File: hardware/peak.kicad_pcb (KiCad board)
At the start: 6 copper layers, 35 x 51 mm, 29 parts, among them J1 Conn_Controller, J2 Conn_Buttons, J3 Conn_CAN, J4 Conn_Display, J5 Conn_DEBUG, Q1 AO3400A, U1 ESP32-S3-WROOM-1, U2 TLV76733DRVx, U3 MCP2542FDxMF

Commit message: ✨ Further schematic updates
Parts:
- removed C1, C2, C3: 10uF/10V, Capacitor_SMD:C_0805_2012Metric
- removed C10, C8, C9: 100nF, Capacitor_SMD:C_0603_1608Metric
- removed C4: 1uF, Capacitor_SMD:C_0603_1608Metric
- removed C7: 1uF/10V, Capacitor_SMD:C_0805_2012Metric
- removed J1: Conn_Controller, Connector_Molex:Molex_PicoBlade_53261-0471_1x04-1MP_P1.25mm_Horizontal
- removed J2: Conn_Buttons, Connector_Molex:Molex_PicoBlade_53261-0471_1x04-1MP_P1.25mm_Horizontal
- removed J3: Conn_CAN, Connector_Molex:Molex_PicoBlade_53261-0271_1x02-1MP_P1.25mm_Horizontal
- removed J4: Conn_Display, lib:ST7789V2
- removed J5: Conn_DEBUG, lib:DEBUG_SMD
- removed Q1: AO3400A, PCM_Package_TO_SOT_SMD_AKL:SOT-23
- removed R2: 10k, PCM_Resistor_SMD_AKL:R_0603_1608Metric
- removed R4: 5R, PCM_Resistor_SMD_AKL:R_0805_2012Metric
- added U4: TPS62A04ADRL, Package_TO_SOT_SMD:SOT-563, F.Cu at (21.8, 16.8)
- added U6: AP3019AKTR, Package_TO_SOT_SMD:SOT-23-6, F.Cu at (17.1, 22.2)
- added U7: W25Q128JVP, Package_SON:WSON-8-1EP_6x5mm_P1.27mm_EP3.4x4.3mm, F.Cu at (3.73, 15.0)
- added U8: MCP1700T-2502E-TT, PCM_Package_TO_SOT_SMD_AKL:SOT-23, F.Cu at (22.0, 22.2)
- U1: value ESP32-S3-WROOM-1 -> ~; footprint RF_Module:ESP32-S3-WROOM-1 -> PCM_Espressif:ESP32-P4
- U2: value TLV76733DRVx -> AP63203WU; footprint Package_SON:WSON-6-1EP_2x2mm_P0.65mm_EP1x1.6mm_ThermalVias -> PCM_Package_TO_SOT_SMD_AKL:TSOT-23-6
- moved U1 168.0 mm to (6.40, 5.62)
- moved R1 167.5 mm to (16.6, 0.86), turned to 0 degrees
- moved R3 166.0 mm to (16.6, 3.58), turned to 0 degrees
- moved U2 160.9 mm to (17.3, 17.5)
- moved C5 159.7 mm to (20.6, 0.76), turned to 0 degrees
- moved C6 159.0 mm to (20.6, 3.27), turned to 0 degrees
- moved U3 158.0 mm to (25.8, 1.88), turned to 0 degrees
- moved R5 149.2 mm to (16.6, 6.30), turned to 0 degrees
- moved R6 148.6 mm to (16.6, 9.02), turned to 0 degrees
- moved R7 148.0 mm to (16.6, 11.7), turned to 0 degrees
- moved C11 143.5 mm to (20.6, 5.78), turned to 0 degrees
- moved C12 142.9 mm to (20.6, 8.29), turned to 0 degrees
- moved C13 142.3 mm to (20.6, 10.8), turned to 0 degrees
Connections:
- U1 pad 1: GND -> unconnected-(U1-GPIO1/ADC-Pad1)
- U1 pad 10: /TXD -> unconnected-(U1-GPIO9/ADC-Pad10)
- U1 pad 11: /RXD -> unconnected-(U1-GPIO10/ADC-Pad11)
- U1 pad 12: /BACKLIGHT -> unconnected-(U1-GPIO11/ADC-Pad12)
- U1 pad 18: /CS -> unconnected-(U1-GPIO17/ADC-Pad18)
- U1 pad 19: /SDA -> unconnected-(U1-GPIO18/ADC-Pad19)
- U1 pad 2: +3.3V -> unconnected-(U1-GPIO2/ADC-Pad2)
- U1 pad 20: /SCL -> unconnected-(U1-GPIO19/ADC-Pad20)
- U1 pad 21: unconnected-(U1-IO13-Pad21) -> +3.3V
- U1 pad 26: unconnected-(U1-IO45-Pad26) -> +1V2
- U1 pad 27: /BOOT -> /MCU/FLASH_CS
- U1 pad 28: unconnected-(U1-IO35-Pad28) -> /MCU/FLASH_Q
- U1 pad 29: unconnected-(U1-IO36-Pad29) -> /MCU/FLASH_WP
- U1 pad 3: /EN -> unconnected-(U1-GPIO3/ADC-Pad3)
- U1 pad 30: unconnected-(U1-IO37-Pad30) -> +3.3V
- U1 pad 31: unconnected-(U1-IO38-Pad31) -> /MCU/FLASH_HOLD
- U1 pad 32: unconnected-(U1-IO39-Pad32) -> /MCU/FLASH_CK
- U1 pad 33: unconnected-(U1-IO40-Pad33) -> /MCU/FLASH_D
- U1 pad 36: /RX0 -> unconnected-(U1-DSI_DATAN1-Pad36)
- U1 pad 37: /TX0 -> unconnected-(U1-DSI_CLKN-Pad37)
- U1 pad 38: /DC -> unconnected-(U1-DSI_CLKP-Pad38)
- U1 pad 4: /RESET -> unconnected-(U1-GPIO4/ADC-Pad4)
- U1 pad 40: GND -> unconnected-(U1-DSI_DATAN0-Pad40)
- U1 pad 41: GND -> +2V5
- U1 pad 5: /BUTTON_D -> unconnected-(U1-GPIO5/ADC-Pad5)
- U1 pad 6: /BUTTON_U -> unconnected-(U1-GPIO6/ADC-Pad6)
- U1 pad 7: /BUTTON_P -> unconnected-(U1-GPIO7/ADC-Pad7)
- U1 pad 9: unconnected-(U1-IO16-Pad9) -> +3.3V
- U2 pad 2: +3.3V -> +5V
- U2 pad 3: GND -> +5V
- U2 pad 4: +5V -> GND
- U2 pad 5: GND -> Net-(U2-SW)
- U2 pad 6: +5V -> Net-(U2-BST)
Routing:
- net /BUTTON_D: track 48.6 -> 0.00 mm, vias 2 -> 0
- net /BUTTON_U: track 47.3 -> 0.00 mm, vias 2 -> 0
- net /BUTTON_P: track 45.9 -> 0.00 mm, vias 2 -> 0
- net /CAN_L: track 41.0 -> 0.00 mm, vias 2 -> 0
- net /CAN_H: track 40.9 -> 0.00 mm
- net /DC: track 33.3 -> 0.00 mm, vias 1 -> 0
- net /RESET: track 29.9 -> 0.00 mm, vias 1 -> 0
- net /EN: track 28.4 -> 0.00 mm, vias 2 -> 0
- net +3.3V: track 18.3 -> 0.00 mm, vias 7 -> 0
- net /TXD: track 18.3 -> 0.00 mm, vias 2 -> 0
- net /RXD: track 18.0 -> 0.00 mm, vias 2 -> 0
- net /SDA: track 13.7 -> 0.00 mm, vias 1 -> 0
- net /CS: track 12.7 -> 0.00 mm, vias 1 -> 0
- net /BOOT: track 12.7 -> 0.00 mm
- net /SCL: track 12.2 -> 0.00 mm, vias 1 -> 0
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- removed copper zone on F.Cu, net +3.3V
- removed copper zone on In3.Cu, net +3.3V
- removed copper zone on F.Cu, net +5V
- removed copper zone on In3.Cu, net +5V
- removed copper zone on B.Cu, net GND
- removed copper zone on F.Cu, net GND
- removed copper zone on In1.Cu, net GND
- removed copper zone on In4.Cu, net GND
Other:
- board outline removed
- copper layers 6 -> 4
- board text removed: "3.3V"
- board text removed: "BUTTONS"
- board text removed: "CAN"
- board text removed: "CTRL"
- board text removed: "DEBUG"
- board text removed: "LED"

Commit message: 📂 PCB updates
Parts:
- added C1: 10uF, Capacitor_SMD:C_0805_2012Metric, F.Cu at (188.4, 79.9)
- added C14: 100nF/100V, Capacitor_SMD:C_0805_2012Metric, F.Cu at (193.1, 106.8)
- added C15: 10uF/100V, Capacitor_SMD:C_1206_3216Metric, F.Cu at (189.7, 101.7)
- added C16: 10uF/100V, Capacitor_SMD:C_1206_3216Metric, F.Cu at (189.7, 104.0)
- added C17: 100nF/100V, Capacitor_SMD:C_0805_2012Metric, F.Cu at (188.3, 92.7)
- added C18: 1uF, Capacitor_SMD:C_0402_1005Metric, F.Cu at (201.1, 88.1)
- added C2: 100nF/50V, Capacitor_SMD:C_0603_1608Metric, F.Cu at (190.9, 79.6)
- added C20: 22uF, Capacitor_SMD:C_0805_2012Metric, F.Cu at (194.9, 89.0)
- added C21: 22uF, Capacitor_SMD:C_0805_2012Metric, F.Cu at (194.9, 87.0)
- added C22: 22uF, Capacitor_SMD:C_0805_2012Metric, F.Cu at (194.9, 85.0)
- added C23: 10uF, Capacitor_SMD:C_0805_2012Metric, F.Cu at (227.9, 78.9)
- added C24: 4.7nF, Capacitor_SMD:C_0603_1608Metric, F.Cu at (224.2, 79.1)
- added C25: 22uF, Capacitor_SMD:C_0805_2012Metric, F.Cu at (226.0, 85.0)
- added C26: 22uF, Capacitor_SMD:C_0805_2012Metric, F.Cu at (228.0, 85.0)
- added C27: 4.7uF, Capacitor_SMD:C_0603_1608Metric, F.Cu at (228.8, 90.2)
- added C28: 0.22uF/50V, Capacitor_SMD:C_0805_2012Metric, F.Cu at (228.5, 93.5)
- added C29: 100nF, Capacitor_SMD:C_0402_1005Metric, F.Cu at (202.6, 98.2)
- added C3: 22uF, Capacitor_SMD:C_0805_2012Metric, F.Cu at (195.1, 80.6)
- added C30: 1uF, Capacitor_SMD:C_0603_1608Metric, F.Cu at (221.4, 83.6)
- added C31: 1uF, Capacitor_SMD:C_0603_1608Metric, F.Cu at (216.3, 83.6)
- added C32: 1uF, Capacitor_SMD:C_0603_1608Metric, F.Cu at (198.8, 81.0)
- added C33: 4.7uF, Capacitor_SMD:C_0603_1608Metric, F.Cu at (198.8, 83.0)
- added C34: 100nF, Capacitor_SMD:C_0603_1608Metric, F.Cu at (228.7, 122.3)
- added C35: 100nF, Capacitor_SMD:C_0603_1608Metric, F.Cu at (228.7, 125.3)
- added C36: 100nF, Capacitor_SMD:C_0603_1608Metric, F.Cu at (228.7, 123.8)
- added C37: 100nF, Capacitor_SMD:C_0603_1608Metric, F.Cu at (226.3, 128.2)
- added C38: 100nF, Capacitor_SMD:C_0603_1608Metric, B.Cu at (211.1, 64.0)
- added C39: 12pF, Capacitor_SMD:C_0402_1005Metric, F.Cu at (203.1, 82.8)
- added C4: 22uF, Capacitor_SMD:C_0805_2012Metric, F.Cu at (193.0, 80.5)
- added C40: 12pF, Capacitor_SMD:C_0402_1005Metric, F.Cu at (207.2, 82.8)
- added C41: 1uF, Capacitor_SMD:C_0402_1005Metric, F.Cu at (216.4, 91.1)
- added C42: 1uF, Capacitor_SMD:C_0402_1005Metric, F.Cu at (216.4, 90.1)
- added C43: 1uF, Capacitor_SMD:C_0402_1005Metric, F.Cu at (216.4, 89.1)
- added C44: 1uF, Capacitor_SMD:C_0402_1005Metric, F.Cu at (216.4, 88.1)
- added C45: 100nF, Capacitor_SMD:C_0402_1005Metric, F.Cu at (213.6, 99.3)
- added C46: 100nF, Capacitor_SMD:C_0402_1005Metric, F.Cu at (213.9, 84.6)
- added C47: 100nF, Capacitor_SMD:C_0402_1005Metric, F.Cu at (216.4, 93.1)
- added C48: 100nF, Capacitor_SMD:C_0402_1005Metric, F.Cu at (216.4, 95.1)
- added C49: 100nF, Capacitor_SMD:C_0402_1005Metric, F.Cu at (209.4, 84.6)
- added C50: 100nF, Capacitor_SMD:C_0402_1005Metric, F.Cu at (201.1, 91.1)
- added C51: 100nF, Capacitor_SMD:C_0402_1005Metric, F.Cu at (216.4, 94.1)
- added C52: 100nF, Capacitor_SMD:C_0402_1005Metric, F.Cu at (212.6, 99.3)
- added C53: 100nF, Capacitor_SMD:C_0402_1005Metric, F.Cu at (210.4, 84.6)
- added C54: 100nF, Capacitor_SMD:C_0402_1005Metric, F.Cu at (201.1, 89.1)
- added C55: 100nF, Capacitor_SMD:C_0402_1005Metric, F.Cu at (212.9, 84.6)
- added C56: 100nF, Capacitor_SMD:C_0402_1005Metric, F.Cu at (216.4, 87.1)
- added C57: 100nF, Capacitor_SMD:C_0402_1005Metric, F.Cu at (201.1, 86.1)
- added C58: 100nF, Capacitor_SMD:C_0402_1005Metric, F.Cu at (201.1, 85.1)
- added C59: 100nF, Capacitor_SMD:C_0402_1005Metric, F.Cu at (208.4, 84.6)
- added C60: 100nF, Capacitor_SMD:C_0402_1005Metric, F.Cu at (201.1, 90.1)
- added C61: 10uF, Capacitor_SMD:C_0603_1608Metric, F.Cu at (199.5, 71.3)
- added C62: 1uF, Capacitor_SMD:C_0603_1608Metric, F.Cu at (199.5, 76.0)
- added C7: 1uF/100V, Capacitor_SMD:C_1206_3216Metric, F.Cu at (188.5, 97.2)
- added C8: 1uF/100V, Capacitor_SMD:C_1206_3216Metric, F.Cu at (190.8, 97.2)
- added C9: 1uF/100V, Capacitor_SMD:C_1206_3216Metric, F.Cu at (193.1, 97.2)
- added DZ1: BZX84-C12, PCM_Package_TO_SOT_SMD_AKL:SOT-23, F.Cu at (193.0, 118.7)
- added F2: Fuse, Fuse:Fuse_2512_6332Metric_Pad1.52x3.35mm_HandSolder, F.Cu at (191.4, 110.5)
- added FB1: FerriteBead, Inductor_SMD:L_0805_2012Metric, F.Cu at (201.2, 82.0)
- added FL1: ACT32P-102-2P-TL01, PEAK:ACT32P_TDK, F.Cu at (189.7, 106.9)
- added J1: ~, lib:5034802000, F.Cu at (208.8, 104.4)
- added J2: Conn_DEBUG_C6, Connector_JST:JST_SHL_SM06B-SHLS-TF_1x06-1MP_P1.00mm_Horizontal, F.Cu at (192.2, 71.1)
- added J3: Conn_Buttons, Connector_JST:JST_PH_S4B-PH-SM4-TB_1x04-1MP_P2.00mm_Horizontal, F.Cu at (217.0, 124.8)
- added J4: Conn_DEBUG_P4, Connector_JST:JST_SHL_SM06B-SHLS-TF_1x06-1MP_P1.00mm_Horizontal, F.Cu at (225.4, 71.1)
- added J6: Conn_Controller, Connector_JST:JST_PH_S5B-PH-SM4-TB_1x05-1MP_P2.00mm_Horizontal, F.Cu at (202.5, 124.8)
- added L1: 8.2uH, Inductor_SMD:L_Bourns_SRP5030T, F.Cu at (190.3, 86.9)
- added L2: 3.9uH, Inductor_SMD:L_APV_ANR4030, F.Cu at (194.2, 76.5)
- added L3: 220nH, Inductor_SMD:L_0603_1608Metric, F.Cu at (226.6, 81.7)
- added L4: 15uH, Inductor_SMD:L_1210_3225Metric, F.Cu at (225.7, 90.2)
- added Q1: DMP10H400SE, PCM_Package_TO_SOT_SMD_AKL:SOT-223-3_TabPin2, F.Cu at (191.1, 125.2)
- added Q2: BSS123, PCM_Package_TO_SOT_SMD_AKL:SOT-23, F.Cu at (189.2, 118.7)
- added R10: 100k, Resistor_SMD:R_0603_1608Metric, F.Cu at (224.2, 85.2)
- added R11: 10, Resistor_SMD:R_0805_2012Metric, F.Cu at (225.1, 96.2)
- added R12: 100k, Resistor_SMD:R_0603_1608Metric, F.Cu at (228.3, 96.0)
- added R13: 10k, PCM_Resistor_SMD_AKL:R_0402_1005Metric, F.Cu at (201.1, 92.1)
- added R14: 10k, Resistor_SMD:R_0603_1608Metric, F.Cu at (225.7, 122.3)
- added R15: 10k, Resistor_SMD:R_0603_1608Metric, F.Cu at (225.7, 125.3)
- added R16: 10k, Resistor_SMD:R_0603_1608Metric, F.Cu at (225.7, 123.8)
- added R17: 10k, Resistor_SMD:R_0603_1608Metric, F.Cu at (188.9, 116.0)
- added R18: 1M, Resistor_SMD:R_0603_1608Metric, F.Cu at (198.6, 106.0)
- added R19: 47k, Resistor_SMD:R_0603_1608Metric, F.Cu at (198.6, 103.0)
- added R2: 100k, Resistor_SMD:R_0603_1608Metric, F.Cu at (194.1, 90.9)
- added R20: 1k, Resistor_SMD:R_0603_1608Metric, F.Cu at (197.1, 106.0)
- added R21: 0, PCM_Resistor_SMD_AKL:R_0402_1005Metric, F.Cu at (204.2, 85.0)
- added R22: 0, PCM_Resistor_SMD_AKL:R_0402_1005Metric, F.Cu at (206.1, 85.0)
- added R23: 4.02k, PCM_Resistor_SMD_AKL:R_0402_1005Metric, F.Cu at (205.3, 99.3)
- added R24: 10k, Resistor_SMD:R_0603_1608Metric, F.Cu at (199.5, 74.5)
- added R25: 10k, Resistor_SMD:R_0603_1608Metric, F.Cu at (211.9, 81.5)
- added R26: 0, Resistor_SMD:R_0603_1608Metric, F.Cu at (219.5, 107.4)
- added R27: 0, Resistor_SMD:R_0603_1608Metric, F.Cu at (221.0, 107.4)
- added R28: 0, Resistor_SMD:R_0603_1608Metric, F.Cu at (225.8, 107.4)
- added R29: 0, Resistor_SMD:R_0603_1608Metric, F.Cu at (227.3, 107.4)
- added R30: 51k, Resistor_SMD:R_0603_1608Metric, F.Cu at (218.1, 77.2)
- added R31: 51k, Resistor_SMD:R_0603_1608Metric, F.Cu at (218.1, 75.7)
- added R32: 51k, Resistor_SMD:R_0603_1608Metric, F.Cu at (218.1, 74.2)
- added R33: 51k, Resistor_SMD:R_0603_1608Metric, F.Cu at (218.1, 72.7)
- added R34: 51k, Resistor_SMD:R_0603_1608Metric, F.Cu at (218.1, 78.7)
- added R35: 51k, Resistor_SMD:R_0603_1608Metric, F.Cu at (213.4, 81.5)
- added R36: 0, PCM_Resistor_SMD_AKL:R_0402_1005Metric, F.Cu at (206.3, 99.3)
- added R37: 0, PCM_Resistor_SMD_AKL:R_0402_1005Metric, F.Cu at (207.3, 99.3)
- added R38: 0, PCM_Resistor_SMD_AKL:R_0402_1005Metric, F.Cu at (208.3, 99.3)
- added R39: 0, PCM_Resistor_SMD_AKL:R_0402_1005Metric, F.Cu at (209.3, 99.3)
- added R4: 19.1k, Resistor_SMD:R_0603_1608Metric, F.Cu at (193.5, 93.4)
- added R40: 0, PCM_Resistor_SMD_AKL:R_0402_1005Metric, F.Cu at (210.6, 99.3)
- added R41: 0, PCM_Resistor_SMD_AKL:R_0402_1005Metric, F.Cu at (211.6, 99.3)
- added R42: 4.7k, PCM_Resistor_SMD_AKL:R_0402_1005Metric, F.Cu at (219.3, 94.0)
- added R43: 4.7k, PCM_Resistor_SMD_AKL:R_0402_1005Metric, F.Cu at (219.3, 95.1)
- added R44: 10k, PCM_Resistor_SMD_AKL:R_0402_1005Metric, F.Cu at (201.1, 87.1)
- added R45: 10k, PCM_Resistor_SMD_AKL:R_0402_1005Metric, F.Cu at (216.4, 92.1)
- added R8: 0, Resistor_SMD:R_0603_1608Metric, F.Cu at (192.8, 103.6)
- added R9: 100k, Resistor_SMD:R_0603_1608Metric, F.Cu at (224.2, 82.2)
- added TP1: 5V, TestPoint:TestPoint_Pad_D1.0mm, F.Cu at (198.2, 90.5)
- added TP2: 3.3V, TestPoint:TestPoint_Pad_D1.0mm, F.Cu at (197.8, 78.0)
- added TP3: 1.2V, TestPoint:TestPoint_Pad_D1.0mm, F.Cu at (230.2, 83.9)
- added TP4: LEDA, TestPoint:TestPoint_Pad_D1.0mm, F.Cu at (230.9, 92.5)
- added TP5: 2.5V, TestPoint:TestPoint_Pad_D1.0mm, F.Cu at (218.9, 80.6)
- added TP6: 3.3VA, TestPoint:TestPoint_Pad_D1.0mm, F.Cu at (198.3, 84.9)
- added TP7: VIN, TestPoint:TestPoint_Pad_D1.0mm, F.Cu at (208.8, 129.7)
- added TP8: VBUS, TestPoint:TestPoint_Pad_D1.0mm, F.Cu at (196.8, 110.2)
- added TP9: GND, TestPoint:TestPoint_Pad_D1.0mm, F.Cu at (210.3, 117.9)
- added U10: STS4X, PEAK:STS4X, F.Cu at (228.3, 128.2)
- added U11: LTR-329ALS-01, PEAK:LTR-329ALS-01_LTO, B.Cu at (208.8, 64.0)
- added U12: ESP32-C6-MINI-1/U, PCM_Espressif:ESP32-C6-MINI-1, F.Cu at (208.8, 71.0)
- added U5: PLMR51635XDDCR, Package_TO_SOT_SMD:SOT-23-6, F.Cu at (191.0, 92.7)
- added U9: 74LVC1G17, PCM_Package_TO_SOT_SMD_AKL:SOT-23-5, F.Cu at (220.2, 103.8)
- added X1: ECS-400-10-37B2-CKY-TR, Crystal:Crystal_SMD_2016-4Pin_2.0x1.6mm, F.Cu at (205.1, 83.2)
- C11: value 100nF -> 100nF/100V; footprint Capacitor_SMD:C_0603_1608Metric -> Capacitor_SMD:C_0805_2012Metric
- C13: value 100nF -> 1uF
- R5, R6: value 10k -> 100k; footprint PCM_Resistor_SMD_AKL:R_0603_1608Metric -> Resistor_SMD:R_0805_2012Metric
- R7: value 10k -> 1k; footprint PCM_Resistor_SMD_AKL:R_0603_1608Metric -> Resistor_SMD:R_0603_1608Metric
- moved C5 232.6 mm to (229.0, 104.2), turned to 90 degrees
- moved R1 232.4 mm to (226.5, 100.6)
- moved C6 230.2 mm to (229.0, 101.2), turned to 90 degrees
- moved R3 229.3 mm to (224.0, 101.3), turned to -90 degrees
- moved U3 225.1 mm to (226.5, 103.7), turned to 90 degrees
- moved U6 220.2 mm to (225.5, 93.6)
- moved C12 220.2 mm to (220.3, 101.1)
- moved U1 220.1 mm to (208.8, 92.2)
- moved U4 213.5 mm to (225.9, 79.4), turned to 90 degrees
- moved U7 211.7 mm to (199.4, 96.0), turned to -90 degrees
- moved R5 209.3 mm to (195.4, 115.1), turned to -90 degrees
- moved U8 206.1 mm to (218.8, 83.6)
- moved C11 204.4 mm to (193.4, 115.1), turned to 90 degrees
- moved R6 204.4 mm to (191.3, 115.1), turned to 90 degrees
- moved R7 200.6 mm to (188.9, 114.5), turned to 180 degrees
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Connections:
- net /CAN_H renamed /Connection/CANH
- net /CAN_L renamed /Connection/CANL
- C11 pad 1: /BUTTON_D -> Net-(DZ1-A)
- C12 pad 1: /BUTTON_U -> +3.3V
- C13 pad 1: /BUTTON_P -> Net-(C13-Pad1)
- R5 pad 1: +3.3V -> +BATT
- R5 pad 2: /BUTTON_D -> Net-(DZ1-A)
- R6 pad 1: +3.3V -> Net-(DZ1-A)
- R6 pad 2: /BUTTON_U -> Net-(Q2-D)
- R7 pad 1: +3.3V -> /IO/SW_MCU
- R7 pad 2: /BUTTON_P -> Net-(Q2-G)
- U1 pad 10: unconnected-(U1-GPIO9/ADC-Pad10) -> /IO/SW_MCU
- U1 pad 100: unconnected-(U1-XTAL_P-Pad100) -> /MCU/XTAL_P
- U1 pad 103: unconnected-(U1-CHIP_PU-Pad103) -> /MCU/EN
- U1 pad 15: unconnected-(U1-GPIO14/ADC-Pad15) -> /MCU/SDIO_DATA0
- U1 pad 16: unconnected-(U1-GPIO15/ADC-Pad16) -> /MCU/SDIO_DATA1
- U1 pad 17: unconnected-(U1-GPIO16/ADC-Pad17) -> /MCU/SDIO_DATA2
- U1 pad 18: unconnected-(U1-GPIO17/ADC-Pad18) -> /MCU/SDIO_DATA3
- U1 pad 19: unconnected-(U1-GPIO18/ADC-Pad19) -> /MCU/SDIO_CLK
- U1 pad 20: unconnected-(U1-GPIO19/ADC-Pad20) -> /MCU/SDIO_CMD
- U1 pad 23: unconnected-(U1-GPIO21/ADC-Pad23) -> /MCU/RX1
- U1 pad 24: unconnected-(U1-GPIO22/ADC-Pad24) -> /MCU/TX1
- U1 pad 34: unconnected-(U1-DSI_REXT-Pad34) -> Net-(U1-DSI_REXT)
- U1 pad 35: unconnected-(U1-DSI_DATAP1-Pad35) -> /MCU/MIPI_MCU_D1P
- U1 pad 36: unconnected-(U1-DSI_DATAN1-Pad36) -> /MCU/MIPI_MCU_D1N
- U1 pad 37: unconnected-(U1-DSI_CLKN-Pad37) -> /MCU/MIPI_MCU_CLN
- U1 pad 38: unconnected-(U1-DSI_CLKP-Pad38) -> /MCU/MIPI_MCU_CLP
- U1 pad 39: unconnected-(U1-DSI_DATAP0-Pad39) -> /MCU/MIPI_MCU_D0P
- U1 pad 40: unconnected-(U1-DSI_DATAN0-Pad40) -> /MCU/MIPI_MCU_D0N
- U1 pad 49: unconnected-(U1-USB-DM-Pad49) -> /MCU/JTAG_DN
- U1 pad 50: unconnected-(U1-USB-DP-Pad50) -> /MCU/JTAG_DP
- U1 pad 55: unconnected-(U1-GPIO26/ADC/USB-Pad55) -> /Display/LED_PWM
- U1 pad 56: unconnected-(U1-GPIO27/ADC/USB-Pad56) -> /Display/DISPLAY_TE
- U1 pad 57: unconnected-(U1-GPIO28-Pad57) -> /Display/DISPLAY_RESET
- U1 pad 59: unconnected-(U1-VDD_PSRAM_0-Pad59) -> /MCU/VDDO_PSRAM
- U1 pad 6: unconnected-(U1-GPIO6/ADC-Pad6) -> /Connection/Button_U
- U1 pad 60: unconnected-(U1-GPIO30-Pad60) -> /IO/SCL_MCU
- U1 pad 61: unconnected-(U1-GPIO31-Pad61) -> /IO/SDA_MCU
- U1 pad 66: unconnected-(U1-GPIO35-Pad66) -> /MCU/BOOT
- U1 pad 67: unconnected-(U1-VDD_PSRAM_1-Pad67) -> /MCU/VDDO_PSRAM
- U1 pad 68: unconnected-(U1-GPIO36-Pad68) -> Net-(U1-GPIO36)
- U1 pad 7: unconnected-(U1-GPIO7/ADC-Pad7) -> /Connection/Button_P
- U1 pad 71: unconnected-(U1-VDDO_FLASH-Pad71) -> /MCU/VDDO_FLASH
- U1 pad 72: unconnected-(U1-VDDO_PSRAM-Pad72) -> /MCU/VDDO_PSRAM
- U1 pad 73: unconnected-(U1-VDDO_3-Pad73) -> /MCU/VDDO_3
- U1 pad 74: unconnected-(U1-VDDO_4-Pad74) -> /MCU/VDDO_4
- U1 pad 77: unconnected-(U1-VDD_DCDCC-Pad77) -> +3.3V
- U1 pad 8: unconnected-(U1-GPIO8/ADC-Pad8) -> /Connection/Button_D
- U1 pad 92: unconnected-(U1-GPIO49/ADC-Pad92) -> /IO/VBUS_MCU
- U1 pad 99: unconnected-(U1-XTAL_N-Pad99) -> /MCU/XTAL_N
- U3 pad 1: /TXD -> /MCU/TX1
- U3 pad 4: /RXD -> /MCU/RX1
- U6 pad 3: /Power supply/LED_K -> /Display/LEDK
- U6 pad 4: /Power supply/LED_PWM -> /Display/LED_PWM
- U6 pad 5: /Power supply/LED_A -> /Display/LEDA
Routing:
- net +3.3V: track 0.00 -> 149.4 mm, vias 0 -> 31
- net /IO/SCL_MCU: track 0.00 -> 78.3 mm, vias 0 -> 4
- net /IO/SDA_MCU: track 0.00 -> 78.1 mm, vias 0 -> 4
- net /Connection/Button_U: track 0.00 -> 68.6 mm, vias 0 -> 4
- net /Connection/Button_D: track 0.00 -> 68.4 mm, vias 0 -> 4
- net /Connection/Button_P: track 0.00 -> 67.7 mm, vias 0 -> 4
- net +5V: track 0.00 -> 65.9 mm, vias 0 -> 8
- net +1V2: track 0.00 -> 56.8 mm, vias 0 -> 5
- net +BATT: track 0.00 -> 50.5 mm
- net /Connection/RX/CANH: track 0.00 -> 41.4 mm, vias 0 -> 2
- net /Connection/TX/CANL: track 0.00 -> 40.9 mm, vias 0 -> 2
- net /MCU/EN: track 0.00 -> 37.7 mm, vias 0 -> 2
- net /MCU/SDIO_DATA3: track 0.00 -> 33.8 mm, vias 0 -> 2
- net /MCU/SDIO_DATA2: track 0.00 -> 32.4 mm, vias 0 -> 2
- net /Display/LEDA: track 0.00 -> 30.7 mm, vias 0 -> 2
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- added copper zone on F.Cu, net +1V2
- added copper zone on F.Cu, net +3.3V
- added copper zone on In2.Cu, net +3.3V
- added copper zone on F.Cu, net +5V
- added copper zone on In2.Cu, net +5V
- added copper zone on B.Cu, net GND
- added copper zone on F.Cu, net GND
- added copper zone on In1.Cu, net GND
- added copper zone on In4.Cu, net GND
- added copper zone on F.Cu, net VBUS
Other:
- board outline added: 47 x 69.4 mm
- copper layers 4 -> 6
- board text added: "1.2V"
- board text added: "2.5V"
- board text added: "3.3V"
- board text added: "3.3VA"
- board text added: "5V"
- board text added: "Antenna Area"
- board text added: "BAT"
- board text added: "CAN"
- board text added: "D"
- board text added: "DBG_C6"
- board text added: "DBG_P4"
- board text added: "FLASH"
- board text added: "G"
- board text added: "GND"
- board text added: "I2C"
- board text added: "LED"
- board text added: "LEDA"
- board text added: "P"
- board text added: "R"
- board text added: "RX"
- board text added: "S"
- board text added: "SW"
- board text added: "T"
- board text added: "U"
- board text added: "V"
- board text added: "VBUS"
- board text added: "VIN"
- board text added: "XTAL"

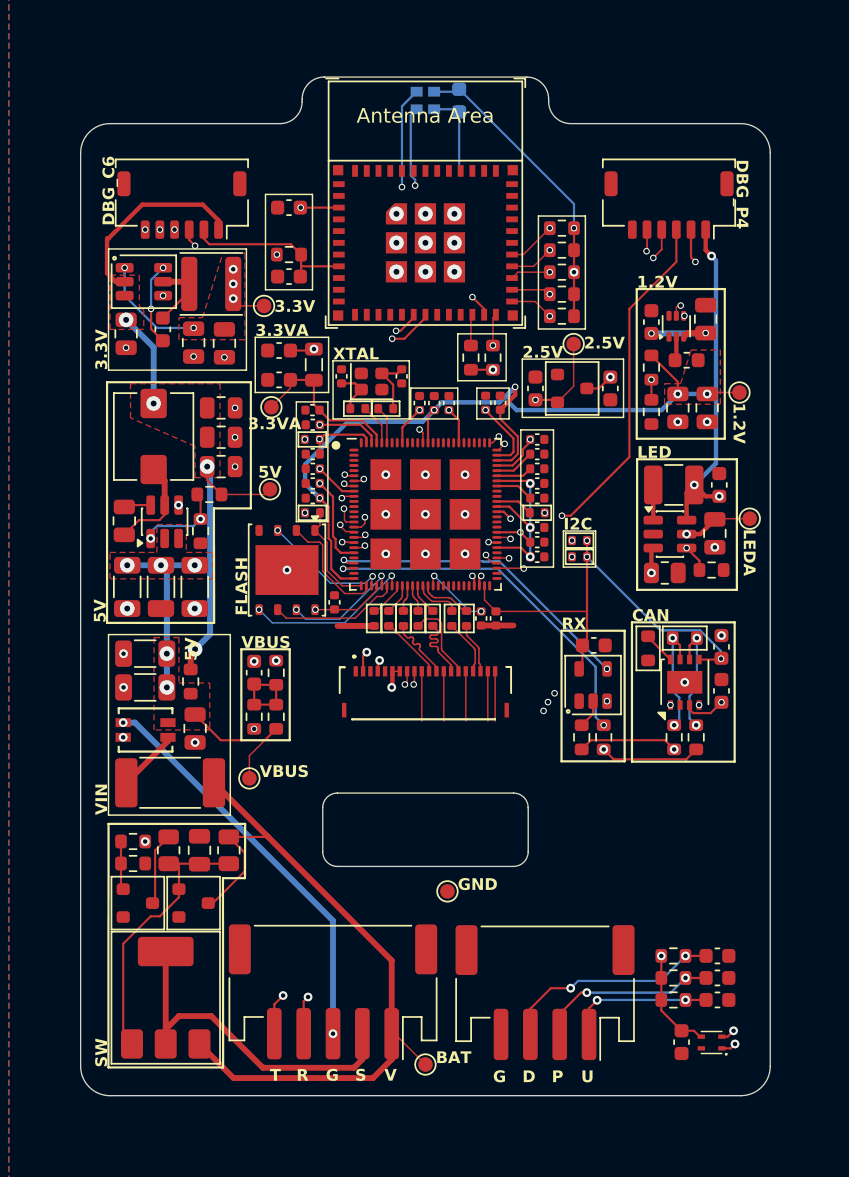
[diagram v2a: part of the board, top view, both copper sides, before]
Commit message: 🐛 Fix errors from rev1.0
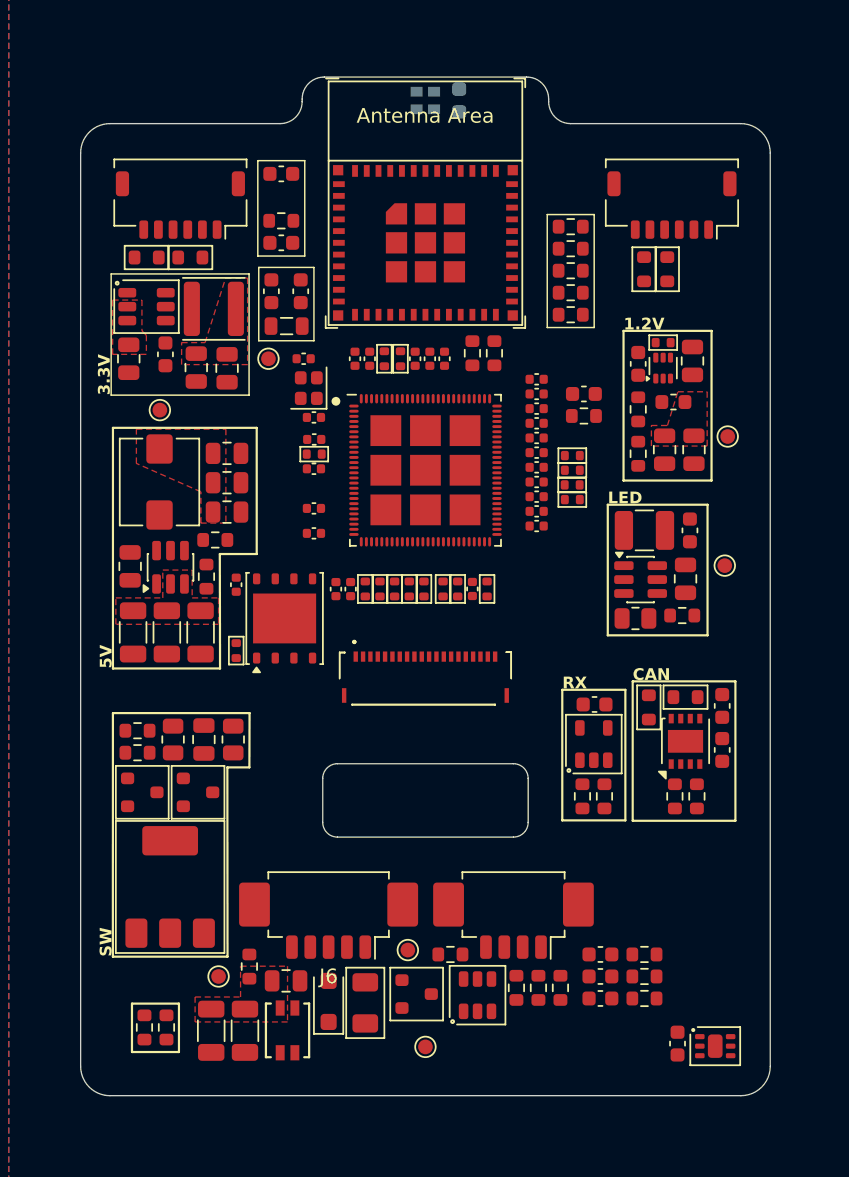
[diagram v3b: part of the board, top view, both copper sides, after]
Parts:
- removed C30: 1uF, Capacitor_SMD:C_0603_1608Metric
- removed C52: 100nF, Capacitor_SMD:C_0402_1005Metric
- removed TP5: 2.5V, TestPoint:TestPoint_Pad_D1.0mm
- removed TP6: 3.3VA, TestPoint:TestPoint_Pad_D1.0mm
- removed U10: STS4X, PEAK:STS4X
- added C10: 100nF, Capacitor_SMD:C_0402_1005Metric, F.Cu at (212.0, 97.3)
- added C19: 100nF, Capacitor_SMD:C_0402_1005Metric, F.Cu at (202.7, 97.3)
- added D1: SMF60A, Diode_SMD:D_SOD-123F, F.Cu at (202.2, 125.4)
- added D2: PESD2CAN / PESD3V3L2BT, PCM_Package_TO_SOT_SMD_AKL:SOT-23, F.Cu at (208.2, 124.9)
- added D3: SRV05-4, PCM_Package_TO_SOT_SMD_AKL:SOT-23-6, F.Cu at (212.4, 125.0)
- added R46: 33, PCM_Resistor_SMD_AKL:R_0603_1608Metric, F.Cu at (223.7, 75.5)
- added R47: 33, PCM_Resistor_SMD_AKL:R_0603_1608Metric, F.Cu at (225.3, 75.5)
- added R48: 4.02k, PCM_Resistor_SMD_AKL:R_0402_1005Metric, F.Cu at (213.0, 97.3)
- added R49: 33, PCM_Resistor_SMD_AKL:R_0603_1608Metric, F.Cu at (192.8, 74.7)
- added R50: 33, PCM_Resistor_SMD_AKL:R_0603_1608Metric, F.Cu at (189.8, 74.7)
- added R51: 10k, PCM_Resistor_SMD_AKL:R_0402_1005Metric, F.Cu at (218.8, 89.2)
- added R52: 100k, Resistor_SMD:R_0603_1608Metric, F.Cu at (210.5, 122.2)
- added R53: 1k, Resistor_SMD:R_0603_1608Metric, F.Cu at (215.0, 124.5)
- added R54: 1k, Resistor_SMD:R_0603_1608Metric, F.Cu at (216.5, 124.5)
- added R55: 1k, Resistor_SMD:R_0603_1608Metric, F.Cu at (218.0, 124.5)
- added R56: 0, PCM_Resistor_SMD_AKL:R_0402_1005Metric, F.Cu at (225.0, 80.5)
- C18: value 1uF -> 100nF
- C31: value 1uF -> 100nF; footprint Capacitor_SMD:C_0603_1608Metric -> Capacitor_SMD:C_0402_1005Metric
- C38: value 100nF -> 1uF
- F2: footprint Fuse:Fuse_2512_6332Metric_Pad1.52x3.35mm_HandSolder -> PCM_Fuse_AKL:Fuse_1206_3216Metric
- J3: footprint Connector_JST:JST_PH_S4B-PH-SM4-TB_1x04-1MP_P2.00mm_Horizontal -> Connector_Molex:Molex_PicoBlade_53261-0471_1x04-1MP_P1.25mm_Horizontal
- J6: footprint Connector_JST:JST_PH_S5B-PH-SM4-TB_1x05-1MP_P2.00mm_Horizontal -> Connector_Molex:Molex_PicoBlade_53261-0571_1x05-1MP_P1.25mm_Horizontal
- R26, R27: value 0 -> 100
- U8: value MCP1700T-2502E-TT -> T117; footprint PCM_Package_TO_SOT_SMD_AKL:SOT-23 -> PCM_Package_DFN_QFN_AKL:DFN-6-1EP_2x2mm_P0.65mm_EP1x1.6mm
- moved U8 45.9 mm to (228.6, 128.5)
- moved R20 30.4 mm to (219.6, 85.5), turned to 0 degrees
- moved C13 29.4 mm to (219.6, 84.0), turned to 0 degrees
- moved C15 26.1 mm to (194.2, 127.4), turned to -90 degrees
- moved R19 25.8 mm to (189.7, 127.2)
- moved C16 24.4 mm to (196.5, 127.4), turned to -90 degrees
- moved FL1 22.6 mm to (199.4, 127.4), turned to -90 degrees
- moved R18 22.5 mm to (191.2, 127.2), turned to -90 degrees
- moved F2 20.0 mm to (204.7, 125.5), turned to -90 degrees
- moved R8 19.8 mm to (196.8, 123.0)
- moved C31 18.6 mm to (203.7, 97.3)
- moved C14 18.3 mm to (199.3, 124.0), turned to 0 degrees
- moved TP8 13.7 mm to (194.7, 123.7)
- moved R13 10.7 mm to (195.9, 101.5), turned to -90 degrees
- moved TP9 10.7 mm to (208.8, 128.5)
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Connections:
- C31 pad 1: +2V5 -> +3.3V
- J2 pad 4: /Wireless/JTAG_DP -> Net-(J2-Pin_4)
- J2 pad 5: /Wireless/JTAG_DN -> Net-(J2-Pin_5)
- J3 pad 1: /Connection/Button_U -> /Connection/Button_U_IN
- J3 pad 2: /Connection/Button_P -> /Connection/Button_P_IN
- J3 pad 3: /Connection/Button_D -> /Connection/Button_D_IN
- J4 pad 4: /MCU/JTAG_DP -> Net-(J4-Pin_4)
- J4 pad 5: /MCU/JTAG_DN -> Net-(J4-Pin_5)
- R10 pad 1: /MCU/FB_DCDC -> Net-(U4-FB)
- R9 pad 2: /MCU/FB_DCDC -> Net-(U4-FB)
- U1 pad 11: unconnected-(U1-GPIO10/ADC-Pad11) -> /Display/LED_PWM
- U1 pad 12: unconnected-(U1-GPIO11/ADC-Pad12) -> /Display/DISPLAY_TE
- U1 pad 13: unconnected-(U1-GPIO12/ADC-Pad13) -> /Display/DISPLAY_RESET
- U1 pad 41: +2V5 -> /MCU/VDDO_3
- U1 pad 48: unconnected-(U1-CSI_REXT-Pad48) -> Net-(U1-CSI_REXT)
- U1 pad 49: /MCU/JTAG_DN -> unconnected-(U1-USB-DM-Pad49)
- U1 pad 5: unconnected-(U1-GPIO5/ADC-Pad5) -> /MCU/C6_WKUP
- U1 pad 50: /MCU/JTAG_DP -> unconnected-(U1-USB-DP-Pad50)
- U1 pad 52: unconnected-(U1-GPIO24/ADC/USB-Pad52) -> /MCU/JTAG_DN
- U1 pad 53: unconnected-(U1-GPIO25/ADC/USB-Pad53) -> /MCU/JTAG_DP
- U1 pad 55: /Display/LED_PWM -> unconnected-(U1-GPIO26/ADC/USB-Pad55)
- U1 pad 56: /Display/DISPLAY_TE -> unconnected-(U1-GPIO27/ADC/USB-Pad56)
- U1 pad 57: /Display/DISPLAY_RESET -> unconnected-(U1-GPIO28-Pad57)
- U12 pad 5: unconnected-(U12-GPIO2/ADC1_CH2-Pad5) -> /MCU/C6_WKUP
- U4 pad 5: /MCU/FB_DCDC -> Net-(U4-FB)
- U8 pad 1: GND -> /IO/SCL_MCU
- U8 pad 2: +2V5 -> GND
- U8 pad 3: +3.3V -> unconnected-(U8-ALERT-Pad3)
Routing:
- net +3.3V: track 149.4 -> 0.00 mm, vias 31 -> 0
- net /IO/SCL_MCU: track 78.3 -> 0.00 mm, vias 4 -> 0
- net /IO/SDA_MCU: track 78.1 -> 0.00 mm, vias 4 -> 0
- net /Connection/Button_U: track 68.6 -> 0.00 mm, vias 4 -> 0
- net /Connection/Button_D: track 68.4 -> 0.00 mm, vias 4 -> 0
- net /Connection/Button_P: track 67.7 -> 0.00 mm, vias 4 -> 0
- net +5V: track 65.9 -> 0.00 mm, vias 8 -> 0
- net +1V2: track 56.8 -> 0.00 mm, vias 5 -> 0
- net +BATT: track 50.5 -> 0.00 mm
- net /Connection/RX/CANH: track 41.4 -> 0.00 mm, vias 2 -> 0
- net /Connection/TX/CANL: track 40.9 -> 0.00 mm, vias 2 -> 0
- net /MCU/EN: track 37.7 -> 0.00 mm, vias 2 -> 0
- net /MCU/SDIO_DATA3: track 33.8 -> 0.00 mm, vias 2 -> 0
- net /MCU/SDIO_DATA2: track 32.4 -> 0.00 mm, vias 2 -> 0
- net /Display/LEDA: track 30.7 -> 0.00 mm, vias 2 -> 0
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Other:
- outline, holes or cut-outs redrawn
- board text removed: "2.5V"
- board text removed: "3.3VA"
- board text removed: "BAT"
- board text removed: "D"
- board text removed: "DBG_C6"
- board text removed: "DBG_P4"
- board text removed: "FLASH"
- board text removed: "G"
- board text removed: "GND"
- board text removed: "I2C"
- board text removed: "LEDA"
- board text removed: "P"
- board text removed: "R"
- board text removed: "S"
- board text removed: "T"
- board text removed: "U"
- board text removed: "V"
- board text removed: "VBUS"
- board text removed: "VIN"
- board text removed: "XTAL"
